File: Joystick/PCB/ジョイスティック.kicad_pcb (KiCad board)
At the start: 2 copper layers, 30 x 30 mm, 3 parts, among them J1 Conn_01x05_Pin

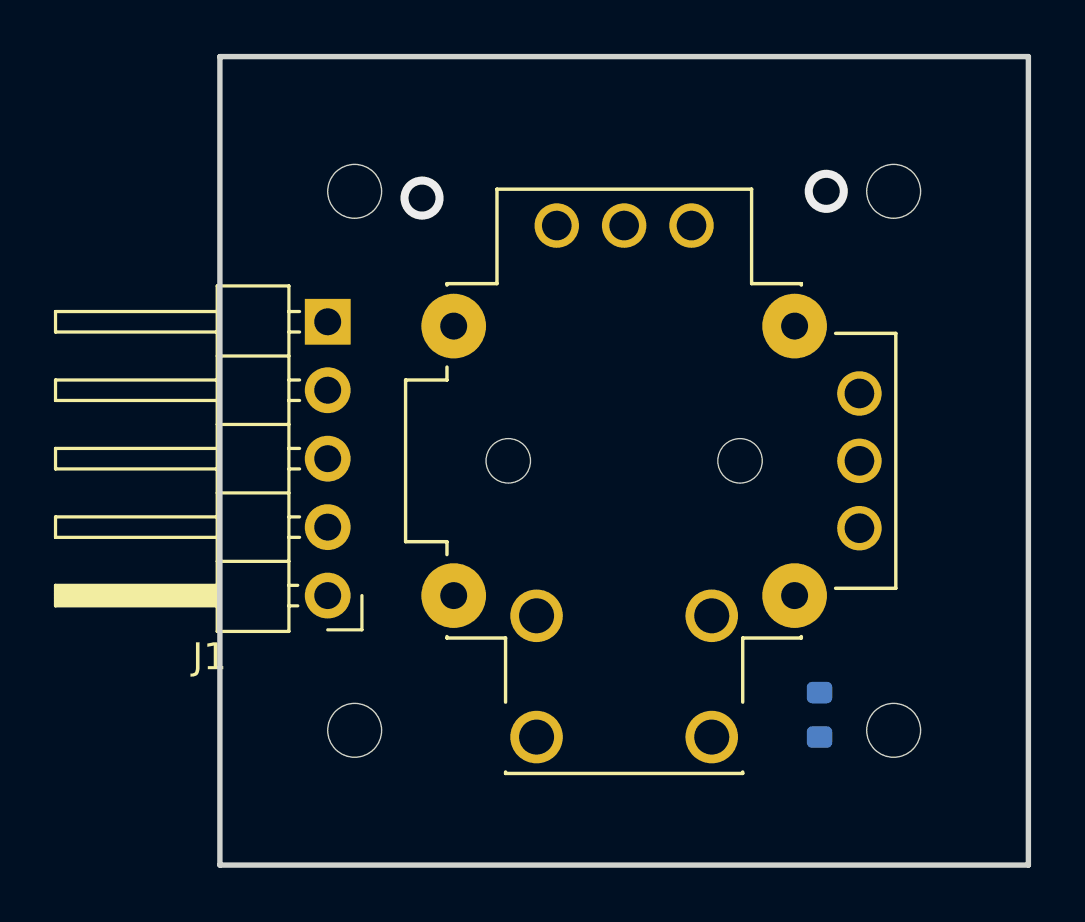
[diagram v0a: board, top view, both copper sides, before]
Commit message: ジョイスティックをセンターに配置
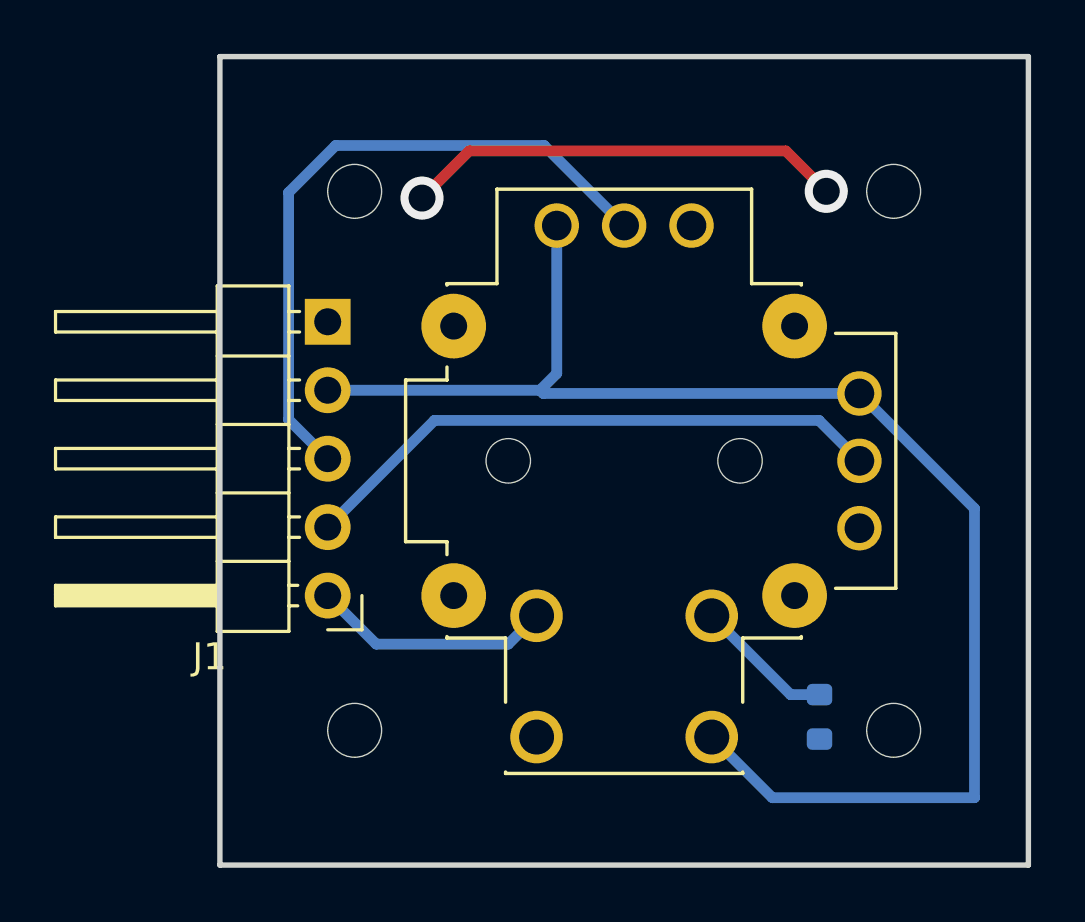
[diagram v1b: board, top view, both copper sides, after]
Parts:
- moved R1 0.07 mm to (127.2, 129.5), turned to -90 degrees
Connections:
- R1 pad 2: /Vin -> GND
- S1 pad B: GND -> /Vin
- S1 pad D: GND -> /Vin
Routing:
- net /Vin: track 0.00 -> 53.6 mm
- net /VR2: track 0.00 -> 24.9 mm
- net /VR1: track 0.00 -> 22.0 mm
- net GND: track 0.00 -> 16.3 mm
- net /SW: track 0.00 -> 14.6 mm
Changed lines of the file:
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@@
 			(psa4output no)
 			(plot_black_and_white yes)
-			(plotinvisibletext no)
 			(sketchpadsonfab no)
 			(plotpadnumbers no)
@@
 			)
 		)
-		(property "Datasheet" ""
+		(property "Datasheet" "~"
 			(at 0 0 180)
 			(unlocked yes)
@@
 			(layers "*.Cu" "*.Mask")
 			(remove_unused_layers no)
-			(net 5 "GND")
+			(net 3 "/Vin")
 			(pinfunction "B")
 			(pintype "passive")
@@
 			(layers "*.Cu" "*.Mask")
 			(remove_unused_layers no)
-			(net 5 "GND")
+			(net 3 "/Vin")
 			(pinfunction "D")
 			(pintype "passive")
@@
 		)
 		(embedded_fonts no)
-		(model "C:/Users/Ryunosuke/Desktop/RKJXV122400R--3DModel-STEP-805722.STEP"
+		(model "${KIPRJMOD}/Lib/RKJXV122400R/RKJXV122400R.step"
 			(offset
 				(xyz 0 0 0)
@@
 	(footprint "Resistor_SMD:R_0603_1608Metric"
 		(layer "B.Cu")
-		(at 127.25 129.425 90)
+		(at 127.25 129.5 -90)
 		(descr "Resistor SMD 0603 (1608 Metric), square (rectangular) end terminal, IPC_7351 nominal, (Body size source: IPC-SM-782 page 72, https://www.pcb-3d.com/wordpress/wp-content/uploads/ipc-sm-782a_amendment_1_and_2.pdf), generated with kicad-footprint-generator")
 		(tags "resistor")
@@
 			)
 		)
-		(property "Datasheet" ""
-			(at 0 0 270)
+		(property "Datasheet" "~"
+			(at 0 0 90)
 			(unlocked yes)
 			(layer "B.Fab")
@@
 		)
 		(property "Description" "Resistor"
-			(at 0 0 270)
+			(at 0 0 90)
 			(unlocked yes)
 			(layer "B.Fab")
@@
 		(attr smd)
 		(fp_line
+			(start -0.237258 0.5225)
+			(end 0.237258 0.5225)
+			(stroke
+				(width 0.12)
+				(type solid)
+			)
+			(layer "B.SilkS")
+		)
+		(fp_line
 			(start -0.237258 -0.5225)
 			(end 0.237258 -0.5225)
@@
 		)
 		(fp_line
-			(start -0.237258 0.5225)
-			(end 0.237258 0.5225)
-			(stroke
-				(width 0.12)
-				(type solid)
-			)
-			(layer "B.SilkS")
+			(start -1.48 0.73)
+			(end 1.48 0.73)
+			(stroke
+				(width 0.05)
+				(type solid)
+			)
+			(layer "B.CrtYd")
+		)
+		(fp_line
+			(start 1.48 0.73)
+			(end 1.48 -0.73)
+			(stroke
+				(width 0.05)
+				(type solid)
+			)
+			(layer "B.CrtYd")
+		)
+		(fp_line
+			(start -1.48 -0.73)
+			(end -1.48 0.73)
+			(stroke
+				(width 0.05)
+				(type solid)
+			)
+			(layer "B.CrtYd")
 		)
 		(fp_line
@@
 		)
 		(fp_line
-			(start -1.48 -0.73)
-			(end -1.48 0.73)
-			(stroke
-				(width 0.05)
-				(type solid)
-			)
-			(layer "B.CrtYd")
-		)
-		(fp_line
-			(start 1.48 0.73)
-			(end 1.48 -0.73)
-			(stroke
-				(width 0.05)
-				(type solid)
-			)
-			(layer "B.CrtYd")
-		)
-		(fp_line
-			(start -1.48 0.73)
-			(end 1.48 0.73)
-			(stroke
-				(width 0.05)
-				(type solid)
-			)
-			(layer "B.CrtYd")
+			(start -0.8 0.4125)
+			(end 0.8 0.4125)
+			(stroke
+				(width 0.1)
+				(type solid)
+			)
+			(layer "B.Fab")
+		)
+		(fp_line
+			(start 0.8 0.4125)
+			(end 0.8 -0.4125)
+			(stroke
+				(width 0.1)
+				(type solid)
+			)
+			(layer "B.Fab")
+		)
+		(fp_line
+			(start -0.8 -0.4125)
+			(end -0.8 0.4125)
+			(stroke
+				(width 0.1)
+				(type solid)
+			)
+			(layer "B.Fab")
 		)
 		(fp_line
 			(start 0.8 -0.4125)
 			(end -0.8 -0.4125)
-			(stroke
-				(width 0.1)
-				(type solid)
-			)
-			(layer "B.Fab")
-		)
-		(fp_line
-			(start -0.8 -0.4125)
-			(end -0.8 0.4125)
-			(stroke
-				(width 0.1)
-				(type solid)
-			)
-			(layer "B.Fab")
-		)
-		(fp_line
-			(start 0.8 0.4125)
-			(end 0.8 -0.4125)
-			(stroke
-				(width 0.1)
-				(type solid)
-			)
-			(layer "B.Fab")
-		)
-		(fp_line
-			(start -0.8 0.4125)
-			(end 0.8 0.4125)
 			(stroke
 				(width 0.1)
@@
 		)
 		(pad "1" smd roundrect
-			(at -0.825 0 90)
+			(at -0.825 0 270)
 			(size 0.8 0.95)
 			(layers "B.Cu" "B.Mask" "B.Paste")
@@
 		)
 		(pad "2" smd roundrect
-			(at 0.825 0 90)
+			(at 0.825 0 270)
 			(size 0.8 0.95)
 			(layers "B.Cu" "B.Mask" "B.Paste")
 			(roundrect_rratio 0.25)
-			(net 3 "/Vin")
+			(net 5 "GND")
 			(pintype "passive")
 		)
@@
 		(fill no)
 		(layer "Edge.Cuts")
+	)
+	(segment
+		(start 115.699 126.801)
+		(end 116.75 125.75)
+		(width 0.4)
+		(layer "B.Cu")
+		(net 1)
+	)
+	(segment
+		(start 126.175 128.675)
+		(end 127.25 128.675)
+		(width 0.4)
+		(layer "B.Cu")
+		(net 1)
+	)
+	(segment
+		(start 109 125)
+		(end 110.801 126.801)
+		(width 0.4)
+		(layer "B.Cu")
+		(net 1)
+	)
+	(segment
+		(start 123.25 125.75)
+		(end 126.175 128.675)
+		(width 0.4)
+		(layer "B.Cu")
+		(net 1)
+	)
+	(segment
+		(start 110.801 126.801)
+		(end 115.699 126.801)
+		(width 0.4)
+		(layer "B.Cu")
+		(net 1)
+	)
+	(segment
+		(start 123.25 125.75)
+		(end 123.25 126.25)
+		(width 0.4)
+		(layer "B.Cu")
+		(net 1)
+	)
+	(segment
+		(start 109.295422 108.299)
+		(end 117.029 108.299)
+		(width 0.4)
+		(layer "B.Cu")
+		(net 2)
+	)
+	(segment
+		(start 107.549 110.045422)
+		(end 109.295422 108.299)
+		(width 0.4)
+		(layer "B.Cu")
+		(net 2)
+	)
+	(segment
+		(start 109 119.92)
+		(end 107.549 118.469)
+		(width 0.4)
+		(layer "B.Cu")
+		(net 2)
+	)
+	(segment
+		(start 117.029 108.299)
+		(end 120 111.27)
+		(width 0.4)
+		(layer "B.Cu")
+		(net 2)
+	)
+	(segment
+		(start 107.549 118.469)
+		(end 107.549 110.045422)
+		(width 0.4)
+		(layer "B.Cu")
+		(net 2)
+	)
+	(segment
+		(start 117 117.5)
+		(end 116.88 117.38)
+		(width 0.4)
+		(layer "B.Cu")
+		(net 3)
+	)
+	(segment
+		(start 128.73 117.5)
+		(end 117 117.5)
+		(width 0.4)
+		(layer "B.Cu")
+		(net 3)
+	)
+	(segment
+		(start 125.5 132.5)
+		(end 123.25 130.25)
+		(width 0.4)
+		(layer "B.Cu")
+		(net 3)
+	)
+	(segment
+		(start 117.5 116.76)
+		(end 117.5 111.27)
+		(width 0.4)
+		(layer "B.Cu")
+		(net 3)
+	)
+	(segment
+		(start 133 121.77)
+		(end 133 132.5)
+		(width 0.4)
+		(layer "B.Cu")
+		(net 3)
+	)
+	(segment
+		(start 109 117.38)
+		(end 116.88 117.38)
+		(width 0.4)
+		(layer "B.Cu")
+		(net 3)
+	)
+	(segment
+		(start 133 132.5)
+		(end 125.5 132.5)
+		(width 0.4)
+		(layer "B.Cu")
+		(net 3)
+	)
+	(segment
+		(start 128.73 117.5)
+		(end 133 121.77)
+		(width 0.4)
+		(layer "B.Cu")
+		(net 3)
+	)
+	(segment
+		(start 116.88 117.38)
+		(end 117.5 116.76)
+		(width 0.4)
+		(layer "B.Cu")
+		(net 3)
+	)
+	(segment
+		(start 112.96 118.5)
+		(end 127.23 118.5)
+		(width 0.4)
+		(layer "B.Cu")
+		(net 4)
+	)
+	(segment
+		(start 127.23 118.5)
+		(end 128.73 120)
+		(width 0.4)
+		(layer "B.Cu")
+		(net 4)
+	)
+	(segment
+		(start 109 122.46)
+		(end 112.96 118.5)
+		(width 0.4)
+		(layer "B.Cu")
+		(net 4)
+	)
+	(segment
+		(start 126 108.5)
+		(end 127.5 110)
+		(width 0.4)
+		(layer "F.Cu")
+		(net 5)
+	)
+	(segment
+		(start 112.5 110.25)
+		(end 114.25 108.5)
+		(width 0.4)
+		(layer "F.Cu")
+		(net 5)
+	)
+	(segment
+		(start 114.25 108.5)
+		(end 126 108.5)
+		(width 0.4)
+		(layer "F.Cu")
+		(net 5)
 	)
 	(via
@@
 		(layer "B.Cu")
 		(hatch edge 0.5)
+		(priority 1)
 		(connect_pads
 			(clearance 0.5)
@@
 		(min_thickness 0.25)
 		(filled_areas_thickness no)
-		(fill
+		(fill yes
 			(thermal_gap 0.5)
 			(thermal_bridge_width 0.5)
+		)
+		(polygon
+			(pts
+				(xy 105 105) (xy 105 135) (xy 135 135) (xy 135 105)
+			)
+		)
+	)
+	(zone
+		(net 5)
+		(net_name "GND")
+		(layer "B.Cu")
+		(hatch edge 0.5)
+		(connect_pads
+			(clearance 0.5)
+		)
+		(min_thickness 0.25)
+		(filled_areas_thickness no)
+		(fill yes
+			(thermal_gap 0.5)
+			(thermal_bridge_width 0.5)
